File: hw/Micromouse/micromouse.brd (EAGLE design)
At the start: 60 x 97 mm, 54 parts, among them IC1 DSPIC33FJ64MC804-PT, IC2 DRV8833PWR, J1 GP2Y0A51SK0F, J2 GP2Y0A51SK0F, J3 GP2Y0A41SK0F, SW1 B3F-1000

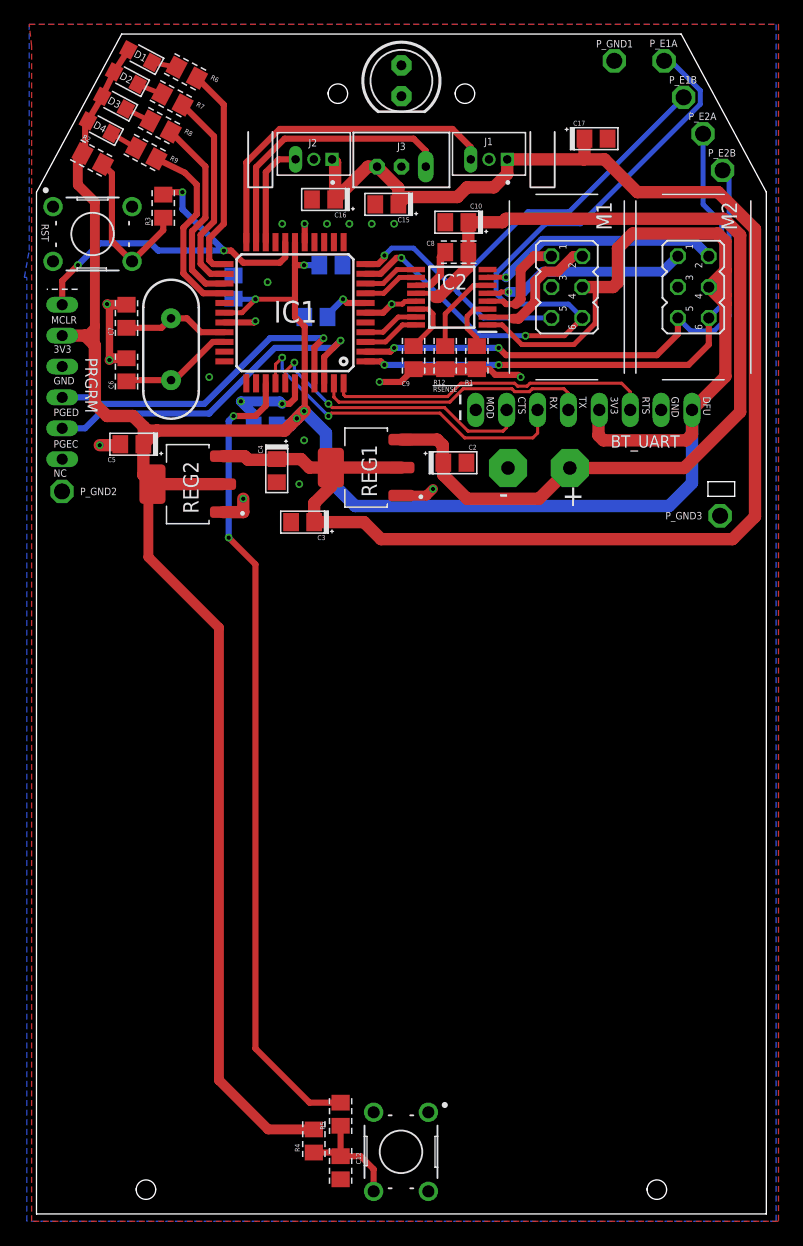
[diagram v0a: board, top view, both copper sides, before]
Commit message: Changed resistor values for LEDS
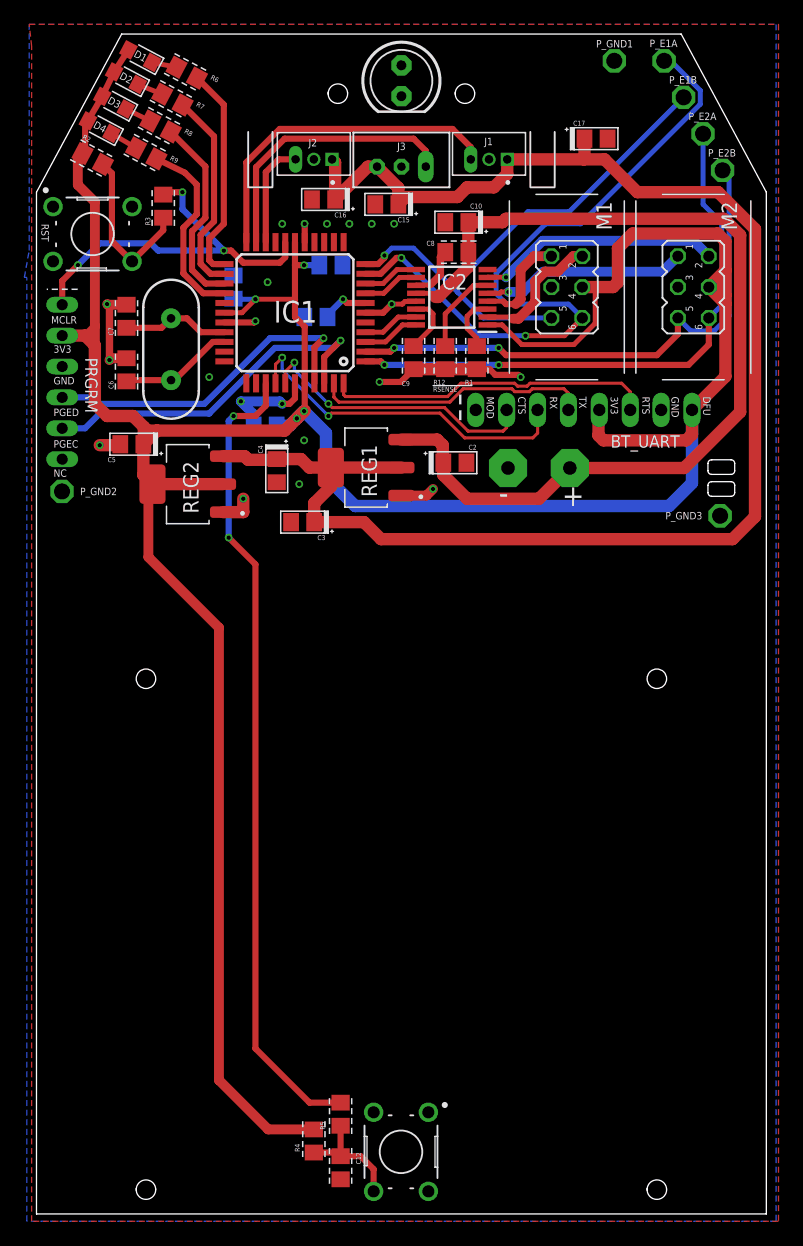
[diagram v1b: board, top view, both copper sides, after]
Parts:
- R6, R7, R8, R9: value 68 -> 820
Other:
- outline, holes or cut-outs redrawn
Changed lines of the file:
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@@
 <drawing>
 <settings>
-<setting alwaysvectorfont="yes"/>
+<setting alwaysvectorfont="no"/>
 <setting verticaltext="up"/>
 </settings>
@@
 </layers>
 <board>
-<fusionsync huburn="a.YnVzaW5lc3M6bXl0dW05MzU" projecturn="a.YnVzaW5lc3M6bXl0dW05MzUjMjAyMTAxMTgzNzI4NzA0MjY" f3durn="urn:adsk.wipprod:dm.lineage:L23jFv8gR_u2aycr5DJv9Q" pcbguid="" lastpulledtime="2021-02-25T09:35:48Z" lastsyncedchangeguid="" latestrevisionid="057abc00-2818-4c85-872c-c5691e58c9ba" lastsyncedrevisionid="057abc00-2818-4c85-872c-c5691e58c9ba" lastboardhashguid="99a244b2-f34e-1964-06c2-123070306d9d" lastpushedtime="2021-02-25T10:11:36Z" linktopcb3d="true"/>
+<fusionsync huburn="a.YnVzaW5lc3M6bXl0dW05MzU" projecturn="a.YnVzaW5lc3M6bXl0dW05MzUjMjAyMTAxMTgzNzI4NzA0MjY" f3durn="urn:adsk.wipprod:dm.lineage:L23jFv8gR_u2aycr5DJv9Q" pcbguid="" lastpulledtime="2021-02-26T11:02:53Z" lastsyncedchangeguid="" latestrevisionid="057abc00-2818-4c85-872c-c5691e58c9ba" lastsyncedrevisionid="3b16979e-9af6-479c-aa9e-43a90bfe8460" lastboardhashguid="99a244b2-f34e-1964-06c2-123070306d9d" lastpushedtime="2021-02-25T10:11:36Z" linktopcb3d="true"/>
 <plain>
 <wire x1="10.598" y1="46.956" x2="10.598" y2="42.498" width="0.1524" layer="21"/>
@@
 <text x="2.6" y="25.6" size="0.4064" layer="21">RSENSE</text>
 <wire x1="2.6" y1="26.1" x2="5.8" y2="26.1" width="0.0762" layer="21"/>
-<wire x1="-20.2065" y1="-39.8911" x2="-21.7947" y2="-39.8998" width="0" layer="20" curve="164.9992"/>
-<wire x1="-20.2065" y1="-39.8911" x2="-20.2" y2="-39.9607" width="0" layer="20"/>
-<wire x1="-21.8" y1="-40.0393" x2="-20.2" y2="-39.9607" width="0" layer="20" curve="180"/>
-<wire x1="-21.8" y1="-40.0393" x2="-21.8" y2="-39.9607" width="0" layer="20"/>
-<wire x1="-21.8" y1="-39.9607" x2="-21.7947" y2="-39.8998" width="0" layer="20"/>
-<wire x1="-6.023" y1="50.0607" x2="-6.023" y2="50.1394" width="0" layer="20"/>
-<wire x1="-6.023" y1="50.1394" x2="-6.0177" y2="50.2002" width="0" layer="20"/>
-<wire x1="-4.4295" y1="50.2089" x2="-6.0177" y2="50.2002" width="0" layer="20" curve="165.0101"/>
+<wire x1="-6.023" y1="50.0607" x2="-6.023" y2="50.1393" width="0" layer="20"/>
+<wire x1="-6.023" y1="50.1393" x2="-6.0177" y2="50.2002" width="0" layer="20"/>
+<wire x1="-4.4295" y1="50.2091" x2="-6.0177" y2="50.2002" width="0" layer="20" curve="165.0026"/>
+<wire x1="-4.4295" y1="50.2091" x2="-4.4295" y2="50.2089" width="0" layer="20"/>
 <wire x1="-4.4295" y1="50.2089" x2="-4.423" y2="50.1393" width="0" layer="20"/>
-<wire x1="-6.023" y1="50.0607" x2="-4.423" y2="50.1393" width="0" layer="20" curve="180.0014"/>
+<wire x1="-6.023" y1="50.0607" x2="-4.423" y2="50.1393" width="0" layer="20" curve="179.9887"/>
+<wire x1="27.1" y1="18.8" x2="27.4" y2="19.1" width="0" layer="20" curve="90"/>
+<wire x1="27.1" y1="18.8" x2="25.5" y2="18.8" width="0" layer="20"/>
+<wire x1="25.2" y1="19.1" x2="25.5" y2="18.8" width="0" layer="20" curve="90"/>
+<wire x1="25.2" y1="19.1" x2="25.2" y2="19.7" width="0" layer="20"/>
+<wire x1="25.5" y1="20" x2="25.2" y2="19.7" width="0" layer="20" curve="90"/>
+<wire x1="25.5" y1="20" x2="27.1" y2="20" width="0" layer="20"/>
+<wire x1="27.4" y1="19.7" x2="27.1" y2="20" width="0" layer="20" curve="90"/>
+<wire x1="27.4" y1="19.7" x2="27.4" y2="19.1" width="0" layer="20"/>
+<wire x1="25.2" y1="17.3" x2="25.5" y2="17" width="0" layer="20" curve="90"/>
+<wire x1="25.2" y1="17.3" x2="25.2" y2="17.9" width="0" layer="20"/>
+<wire x1="25.5" y1="18.2" x2="25.2" y2="17.9" width="0" layer="20" curve="90"/>
+<wire x1="25.5" y1="18.2" x2="27.1" y2="18.2" width="0" layer="20"/>
+<wire x1="27.4" y1="17.9" x2="27.1" y2="18.2" width="0" layer="20" curve="90"/>
+<wire x1="27.4" y1="17.9" x2="27.4" y2="17.3" width="0" layer="20"/>
+<wire x1="27.1" y1="17" x2="27.4" y2="17.3" width="0" layer="20" curve="90"/>
+<wire x1="27.1" y1="17" x2="25.5" y2="17" width="0" layer="20"/>
 <wire x1="20.2" y1="-40.0393" x2="21.8" y2="-39.9607" width="0" layer="20" curve="180"/>
 <wire x1="20.2" y1="-40.0393" x2="20.2" y2="-39.9607" width="0" layer="20"/>
@@
 <wire x1="21.7935" y1="-39.8911" x2="20.2053" y2="-39.8998" width="0" layer="20" curve="164.9993"/>
 <wire x1="21.7935" y1="-39.8911" x2="21.8" y2="-39.9607" width="0" layer="20"/>
+<circle x="21" y="2" radius="0.801" width="0" layer="20"/>
+<circle x="-21" y="2" radius="0.801" width="0" layer="20"/>
+<wire x1="4.423" y1="50.1393" x2="4.4283" y2="50.2003" width="0" layer="20"/>
+<wire x1="6.0165" y1="50.2089" x2="4.4283" y2="50.2003" width="0" layer="20" curve="164.9944"/>
+<wire x1="6.0165" y1="50.2089" x2="6.023" y2="50.1393" width="0" layer="20"/>
+<wire x1="4.423" y1="50.0607" x2="6.023" y2="50.1393" width="0" layer="20" curve="179.9989"/>
 <wire x1="4.423" y1="50.0607" x2="4.423" y2="50.1393" width="0" layer="20"/>
-<wire x1="4.423" y1="50.1393" x2="4.4283" y2="50.2003" width="0" layer="20"/>
-<wire x1="6.0165" y1="50.2089" x2="4.4283" y2="50.2003" width="0" layer="20" curve="164.9935"/>
-<wire x1="6.0165" y1="50.2089" x2="6.023" y2="50.1393" width="0" layer="20"/>
-<wire x1="4.423" y1="50.0607" x2="6.023" y2="50.1393" width="0" layer="20" curve="180.0015"/>
-<wire x1="25.2" y1="17" x2="25.2" y2="18.2" width="0" layer="20"/>
-<wire x1="25.2" y1="18.2" x2="27.4" y2="18.2" width="0" layer="20"/>
-<wire x1="27.4" y1="18.2" x2="27.4" y2="17" width="0" layer="20"/>
-<wire x1="27.4" y1="17" x2="25.2" y2="17" width="0" layer="20"/>
+<wire x1="-20.2065" y1="-39.8911" x2="-21.7947" y2="-39.8998" width="0" layer="20" curve="164.9993"/>
+<wire x1="-20.2065" y1="-39.8911" x2="-20.2" y2="-39.9607" width="0" layer="20"/>
+<wire x1="-21.8" y1="-40.0393" x2="-20.2" y2="-39.9607" width="0" layer="20" curve="179.9998"/>
+<wire x1="-21.8" y1="-40.0393" x2="-21.8" y2="-39.9607" width="0" layer="20"/>
+<wire x1="-21.8" y1="-39.9607" x2="-21.7947" y2="-39.8998" width="0" layer="20"/>
 <wire x1="-23" y1="55" x2="-30" y2="42" width="0" layer="20"/>
 <wire x1="-30" y1="42" x2="-30" y2="-42" width="0" layer="20"/>
@@
 <attribute name="VALUE" x="-3.36" y="-35.07" size="0.4064" layer="27" rot="R90"/>
 </element>
-<element name="R6" library="micromouse" library_urn="urn:adsk.eagle:library:26475156" package="0805" package3d_urn="urn:adsk.eagle:package:26475190/6" value="68" x="-17.6466" y="51.8266" smashed="yes" rot="R332">
+<element name="R6" library="micromouse" library_urn="urn:adsk.eagle:library:26475156" package="0805" package3d_urn="urn:adsk.eagle:package:26475190/6" value="820" x="-17.6466" y="51.8266" smashed="yes" rot="R332">
 <attribute name="NAME" x="-15.73623125" y="51.30785" size="0.4064" layer="25" rot="R332"/>
 <attribute name="VALUE" x="-19.7116" y="51.297303125" size="0.4064" layer="27" rot="R332"/>
 </element>
-<element name="R7" library="micromouse" library_urn="urn:adsk.eagle:library:26475156" package="0805" package3d_urn="urn:adsk.eagle:package:26475190/6" value="68" x="-18.8245" y="49.6145" smashed="yes" rot="R332">
+<element name="R7" library="micromouse" library_urn="urn:adsk.eagle:library:26475156" package="0805" package3d_urn="urn:adsk.eagle:package:26475190/6" value="820" x="-18.8245" y="49.6145" smashed="yes" rot="R332">
 <attribute name="NAME" x="-16.91413125" y="49.09575" size="0.4064" layer="25" rot="R332"/>
 <attribute name="VALUE" x="-20.8895" y="49.085203125" size="0.4064" layer="27" rot="R332"/>
 </element>
-<element name="R8" library="micromouse" library_urn="urn:adsk.eagle:library:26475156" package="0805" package3d_urn="urn:adsk.eagle:package:26475190/6" value="68" x="-19.8" y="47.4024" smashed="yes" rot="R332">
+<element name="R8" library="micromouse" library_urn="urn:adsk.eagle:library:26475156" package="0805" package3d_urn="urn:adsk.eagle:package:26475190/6" value="820" x="-19.8" y="47.4024" smashed="yes" rot="R332">
 <attribute name="NAME" x="-17.88963125" y="46.88365" size="0.4064" layer="25" rot="R332"/>
 <attribute name="VALUE" x="-21.865" y="46.873103125" size="0.4064" layer="27" rot="R332"/>
 </element>
-<element name="R9" library="micromouse" library_urn="urn:adsk.eagle:library:26475156" package="0805" package3d_urn="urn:adsk.eagle:package:26475190/6" value="68" x="-20.9755" y="45.1904" smashed="yes" rot="R332">
+<element name="R9" library="micromouse" library_urn="urn:adsk.eagle:library:26475156" package="0805" package3d_urn="urn:adsk.eagle:package:26475190/6" value="820" x="-20.9755" y="45.1904" smashed="yes" rot="R332">
 <attribute name="NAME" x="-19.06513125" y="44.67165" size="0.4064" layer="25" rot="R332"/>
 <attribute name="VALUE" x="-23.0405" y="44.661103125" size="0.4064" layer="27" rot="R332"/>

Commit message: Finalized board; Added speedy gonzales in the process!
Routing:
- net M2_CHB: track 45.5 -> 59.1 mm
- net M1_CHA: track 58.8 -> 72.5 mm
- net M2_CHA: track 47.4 -> 60.8 mm
- net M1_CHB: track 45.4 -> 54.0 mm
- net MCLR: track 31.5 -> 39.8 mm
- net GND: track 44.4 -> 52.5 mm, vias 21 -> 20
- net N$7: track 13.6 -> 20.2 mm
- net +3V3: track 260.7 -> 266.8 mm
- net UART_RX: track 28.9 -> 34.4 mm
- net BT_CTS: track 23.7 -> 29.2 mm
- net SW1: track 66.8 -> 71.5 mm
- net OSC2: track 9.39 -> 13.3 mm
- net OSC1: track 8.85 -> 12.7 mm
- net N$6: track 9.81 -> 12.6 mm
- net PGED3: track 28.0 -> 30.3 mm
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- added copper zone on layer 16, net MCLR
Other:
- board text added: "MICROMOUSE WISE20/21"
- board text added: "Philipp Hagenlocher Matteo Nardini Hendrik Möller Congnan Wang"
